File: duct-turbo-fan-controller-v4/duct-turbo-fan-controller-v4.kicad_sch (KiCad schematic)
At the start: 45 parts, among them J1 Screw_Terminal_01x04, J2 Conn_01x04, J3 USB_OTG, J4 AudioJack4, J7 Conn_01x04, Q1 MMBT3904, Q2 BSS84, SW1 SW_Push, SW2 SW_Push, U1 SCD41-D-R2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

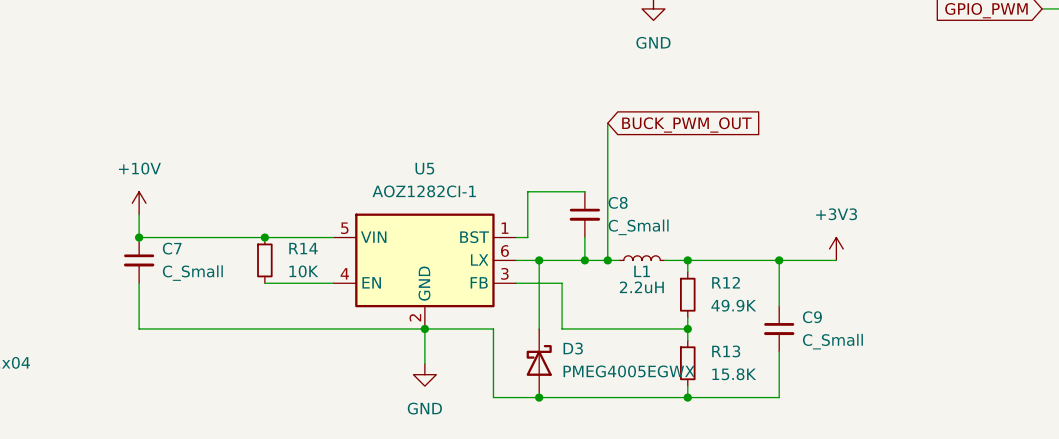
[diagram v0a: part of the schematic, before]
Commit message: Fix footprint for buck diode in schematic.
Add values for buck capacitors in schematic.
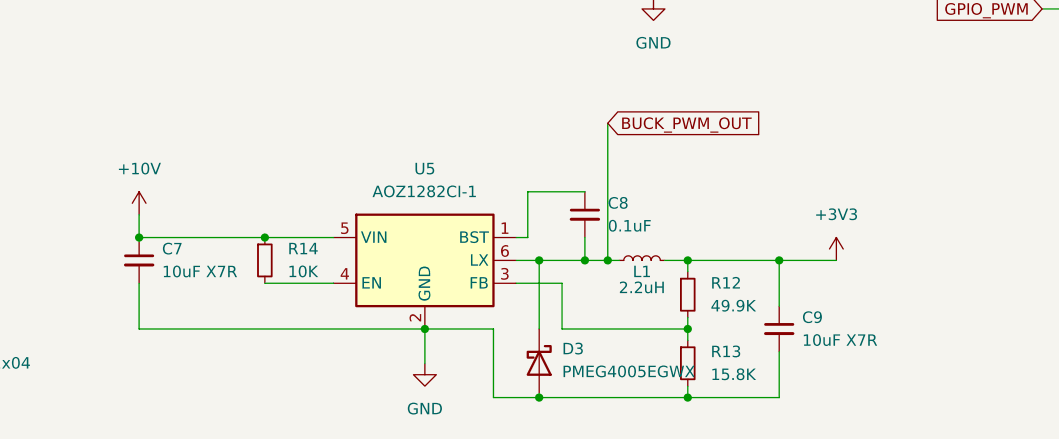
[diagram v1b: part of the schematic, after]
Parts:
- C7, C9: value C_Small -> 10uF X7R
- C8: value C_Small -> 0.1uF
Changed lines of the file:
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@@
 			)
 		)
-		(property "Value" "C_Small"
+		(property "Value" "10uF X7R"
 			(at 158.75 182.8862 0)
 			(effects
@@
 			)
 		)
-		(property "Value" "C_Small"
+		(property "Value" "0.1uF"
 			(at 137.16 170.1862 0)
 			(effects
@@
 			)
 		)
-		(property "Value" "C_Small"
+		(property "Value" "10uF X7R"
 			(at 87.63 175.2662 0)
 			(effects

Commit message: Fix buck diode footprint in pcb
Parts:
- D3: footprint Diode_SMD:D_SOD-323_HandSoldering -> Diode_SMD:D_SOD-123
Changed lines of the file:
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@@
 			)
 		)
-		(property "Footprint" "Diode_SMD:D_SOD-323_HandSoldering"
+		(property "Footprint" "Diode_SMD:D_SOD-123"
 			(at 129.54 185.42 0)
 			(effects

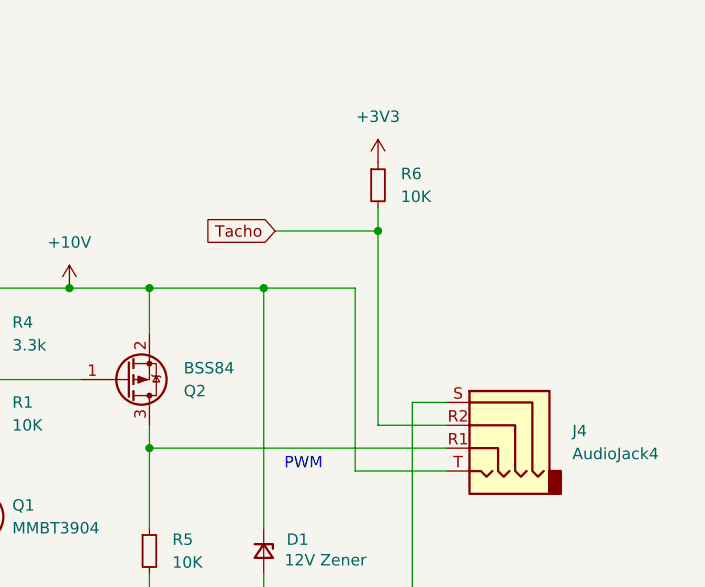
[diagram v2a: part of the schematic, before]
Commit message: Add input resistor from Tacho pin
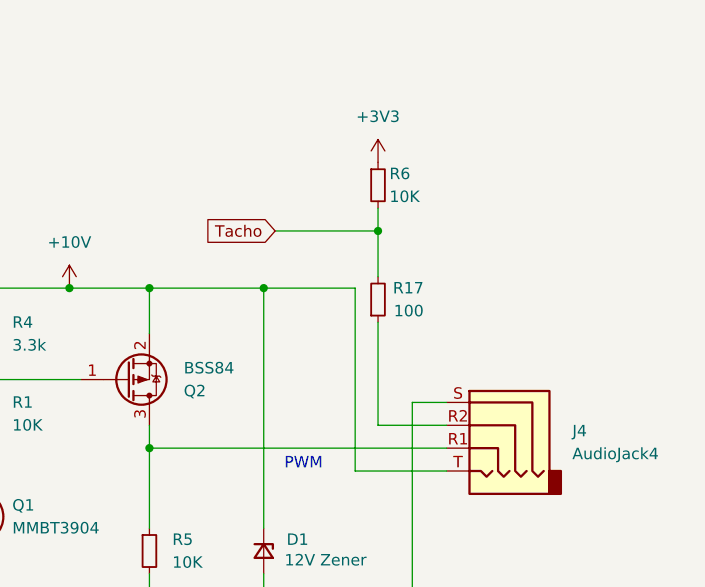
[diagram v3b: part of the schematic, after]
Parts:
- added R17: 100, Resistor_SMD:R_0603_1608Metric_Pad0.98x0.95mm_HandSolder, symbol Device:R_Small
- R6: footprint Resistor_SMD:R_0805_2012Metric_Pad1.20x1.40mm_HandSolder -> Resistor_SMD:R_0603_1608Metric_Pad0.98x0.95mm_HandSolder
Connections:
- net Tacho: now also R17.2; no longer J4.R2
- new net: J4.R2, R17.1
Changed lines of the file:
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@@
 	)
 	(junction
-		(at 142.24 125.73)
+		(at 250.19 114.3)
 		(diameter 0)
 		(color 0 0 0 0)
 	)
 	(junction
-		(at 64.77 26.67)
+		(at 142.24 125.73)
 		(diameter 0)
 		(color 0 0 0 0)
 	)
 	(junction
-		(at 204.47 44.45)
+		(at 64.77 26.67)
 		(diameter 0)
 		(color 0 0 0 0)
 	)
 	(junction
-		(at 171.45 64.77)
+		(at 204.47 44.45)
 		(diameter 0)
 		(color 0 0 0 0)
 	)
 	(junction
-		(at 250.19 114.3)
+		(at 171.45 64.77)
 		(diameter 0)
 		(color 0 0 0 0)
@@
 	(wire
 		(pts
-			(xy 238.76 114.3) (xy 250.19 114.3)
-		)
-		(stroke
-			(width 0)
-			(type default)
-		)
-	)
-	(wire
-		(pts
 			(xy 254 161.29) (xy 237.49 161.29)
 		)
@@
 	(wire
 		(pts
+			(xy 250.19 124.46) (xy 250.19 135.89)
+		)
+		(stroke
+			(width 0)
+			(type default)
+		)
+	)
+	(wire
+		(pts
 			(xy 49.53 26.67) (xy 53.34 26.67)
 		)
@@
 	(wire
 		(pts
+			(xy 250.19 114.3) (xy 250.19 119.38)
+		)
+		(stroke
+			(width 0)
+			(type default)
+		)
+	)
+	(wire
+		(pts
 			(xy 128.27 171.45) (xy 128.27 166.37)
 		)
@@
 	(wire
 		(pts
+			(xy 238.76 114.3) (xy 250.19 114.3)
+		)
+		(stroke
+			(width 0)
+			(type default)
+		)
+	)
+	(wire
+		(pts
 			(xy 196.85 154.94) (xy 196.85 161.29)
 		)
@@
 	(wire
 		(pts
-			(xy 250.19 135.89) (xy 250.19 114.3)
-		)
-		(stroke
-			(width 0)
-			(type default)
-		)
-	)
-	(wire
-		(pts
 			(xy 137.16 173.99) (xy 138.43 173.99)
 		)
@@
 		(on_board yes)
 		(dnp no)
-		(fields_autoplaced yes)
 		(property "Reference" "R6"
-			(at 252.73 107.95 0)
+			(at 251.46 107.95 0)
 			(effects
 				(font
@@
 		)
 		(property "Value" "10K"
-			(at 252.73 110.49 0)
+			(at 251.46 110.49 0)
 			(effects
 				(font
@@
 			)
 		)
-		(property "Footprint" "Resistor_SMD:R_0805_2012Metric_Pad1.20x1.40mm_HandSolder"
+		(property "Footprint" "Resistor_SMD:R_0603_1608Metric_Pad0.98x0.95mm_HandSolder"
 			(at 250.19 109.22 0)
 			(effects
@@
 					(unit 1)
 				)
+			)
+		)
+	)
+	(symbol
+		(lib_id "Device:R_Small")
+		(at 250.19 121.92 0)
+		(mirror x)
+		(unit 1)
+		(exclude_from_sim no)
+		(in_bom yes)
+		(on_board yes)
+		(dnp no)
+		(property "Reference" "R17"
+			(at 255.27 120.65 0)
+			(effects
+				(font
+					(size 1.27 1.27)
+				)
+				(justify right)
+			)
+		)
+		(property "Value" "100"
+			(at 255.27 123.19 0)
+			(effects
+				(font
+					(size 1.27 1.27)
+				)
+				(justify right)
+			)
+		)
+		(property "Footprint" "Resistor_SMD:R_0603_1608Metric_Pad0.98x0.95mm_HandSolder"
+			(at 250.19 121.92 0)
+			(effects
+				(font
+					(size 1.27 1.27)
+				)
+				(hide yes)
+			)
+		)
+		(property "Datasheet" "~"
+			(at 250.19 121.92 0)
+			(effects
+				(font
+					(size 1.27 1.27)
+				)
+				(hide yes)
+			)
+		)
+		(property "Description" ""
+			(at 250.19 121.92 0)
+			(effects
+				(font
+					(size 1.27 1.27)
+				)
+				(hide yes)
+			)
+		)
+		(pin "2"
+		)
+		(pin "1"
+		)
+		(instances
+			(project "duct-turbo-fan-controller-v4"
+				(path "/f7200693-aa8c-4dc9-bbe2-9e962fa196ea"
+					(reference "R17")
+					(unit 1)
+				)

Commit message: Fix bme688 wiring by adding +3.3V to CSB pin.
Was defaulting to spi mode and taking out the whole i2c link
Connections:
- net +3V3: now also R10.2, R11.2, U2.2 (CSB)
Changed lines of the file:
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@@
 (kicad_sch
-	(version 20231120)
+	(version 20250114)
 	(generator "eeschema")
-	(generator_version "8.0")
+	(generator_version "9.0")
 	(paper "A4")
+	(text "PWM"
+		(exclude_from_sim no)
+		(at 239.776 140.97 0)
+		(effects
+			(font
+				(size 1.27 1.27)
+			)
+			(justify left bottom)
+		)
+	)
 	(junction
 		(at 134.62 173.99)
@@
 	)
 	(junction
+		(at 181.61 69.85)
+		(diameter 0)
+		(color 0 0 0 0)
+	)
+	(junction
 		(at 64.77 36.83)
 		(diameter 0)
@@
 	(wire
 		(pts
+			(xy 210.82 69.85) (xy 210.82 66.04)
+		)
+		(stroke
+			(width 0)
+			(type default)
+		)
+	)
+	(wire
+		(pts
 			(xy 146.05 173.99) (xy 156.21 173.99)
 		)
@@
 	(wire
 		(pts
+			(xy 181.61 69.85) (xy 210.82 69.85)
+		)
+		(stroke
+			(width 0)
+			(type default)
+		)
+	)
+	(wire
+		(pts
 			(xy 254 161.29) (xy 237.49 161.29)
 		)
@@
 	(wire
 		(pts
-			(xy 152.4 46.99) (xy 152.4 40.64)
+			(xy 152.4 40.64) (xy 152.4 46.99)
 		)
 		(stroke
@@
 		)
 	)
-	(text "PWM"
-		(exclude_from_sim no)
-		(at 239.776 140.97 0)
-		(effects
-			(font
-				(size 1.27 1.27)
-			)
-			(justify left bottom)
-		)
-	)
 	(global_label "GPIO_PWM"
 		(shape input)
@@
 	(global_label "SCD41_SCA"
 		(shape input)
-		(at 69.85 87.63 0)
+		(at 69.85 87.63 180)
 		(fields_autoplaced yes)
 		(effects
@@
 				(size 1.27 1.27)
 			)
-			(justify left)
+			(justify right)
 		)
 		(property "Intersheetrefs" "${INTERSHEET_REFS}"
-			(at 83.5394 87.63 0)
+			(at 56.1606 87.63 0)
 			(effects
 				(font
 					(size 1.27 1.27)
 				)
-				(justify left)
+				(justify right)
 				(hide yes)
 			)
@@
 	)
 	(symbol
+		(lib_id "power:+3.3V")
+		(at 210.82 66.04 0)
+		(unit 1)
+		(exclude_from_sim no)
+		(in_bom yes)
+		(on_board yes)
+		(dnp no)
+		(fields_autoplaced yes)
+		(property "Reference" "#PWR028"
+			(at 210.82 69.85 0)
+			(effects
+				(font
+					(size 1.27 1.27)
+				)
+				(hide yes)
+			)
+		)
+		(property "Value" "+3V3"
+			(at 210.82 60.96 0)
+			(effects
+				(font
+					(size 1.27 1.27)
+				)
+			)
+		)
+		(property "Footprint" ""
+			(at 210.82 66.04 0)
+			(effects
+				(font
+					(size 1.27 1.27)
+				)
+				(hide yes)
+			)
+		)
+		(property "Datasheet" ""
+			(at 210.82 66.04 0)
+			(effects
+				(font
+					(size 1.27 1.27)
+				)
+				(hide yes)
+			)
+		)
+		(property "Description" ""
+			(at 210.82 66.04 0)
+			(effects
+				(font
+					(size 1.27 1.27)
+				)
+				(hide yes)
+			)
+		)
+		(pin "1"
+		)
+		(instances
+			(project "duct-turbo-fan-controller-v4"
+				(path "/f7200693-aa8c-4dc9-bbe2-9e962fa196ea"
+					(reference "#PWR028")
+					(unit 1)
+				)
+			)
+		)
+	)
+	(symbol
 		(lib_id "Device:R_Small")
 		(at 196.85 152.4 0)
@@
 		)
 	)
+	(embedded_fonts no)
 )

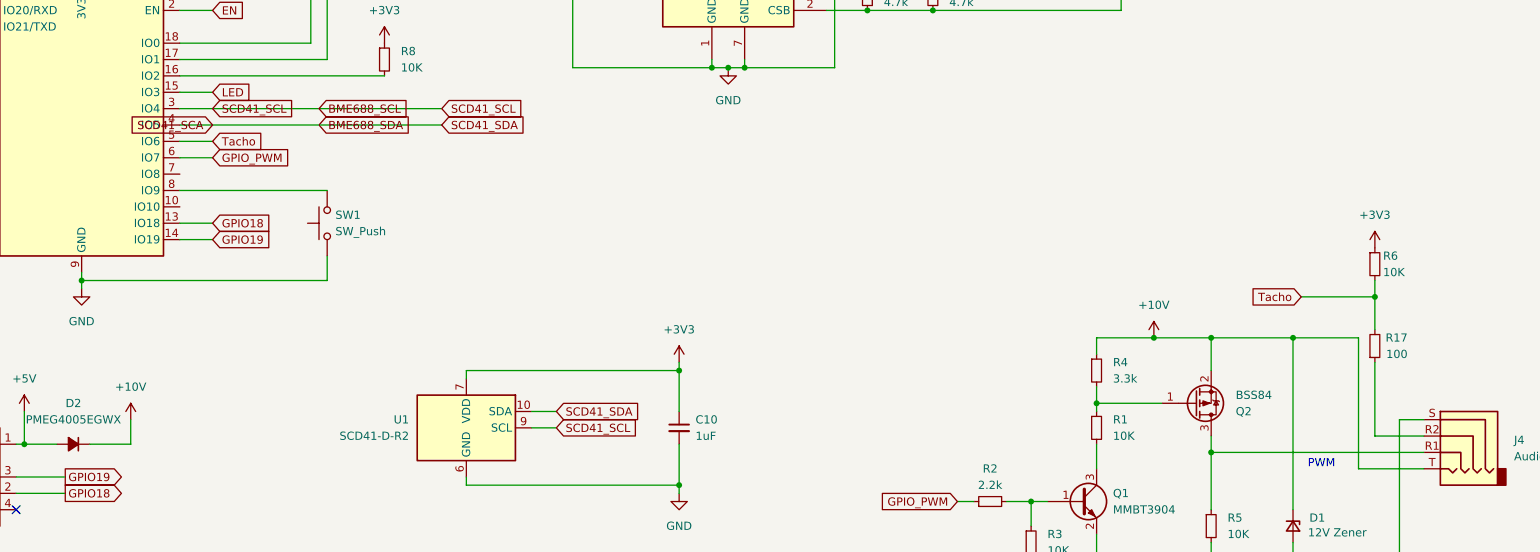
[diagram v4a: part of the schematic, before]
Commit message: Add filter capacitor to input tacho pin.
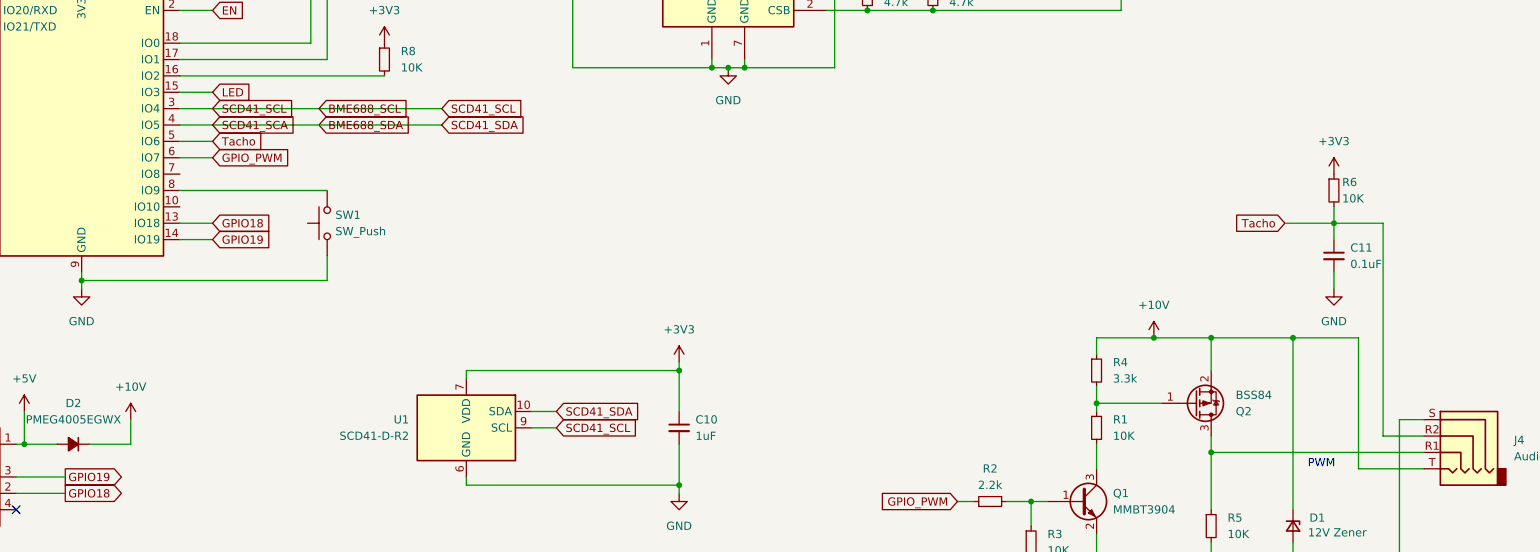
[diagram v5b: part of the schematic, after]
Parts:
- removed R17: 100, Resistor_SMD:R_0603_1608Metric_Pad0.98x0.95mm_HandSolder, symbol Device:R_Small
- added C11: 0.1uF, Capacitor_SMD:C_0603_1608Metric_Pad1.08x0.95mm_HandSolder, symbol Device:C_Small
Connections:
- net GND: now also C11.2
- net Tacho: now also J4.R2, C11.1
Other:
- moved on the sheet: R6
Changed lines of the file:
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@@
 	)
 	(junction
-		(at 250.19 114.3)
+		(at 142.24 125.73)
 		(diameter 0)
 		(color 0 0 0 0)
 	)
 	(junction
-		(at 142.24 125.73)
+		(at 64.77 26.67)
 		(diameter 0)
 		(color 0 0 0 0)
 	)
 	(junction
-		(at 64.77 26.67)
+		(at 243.84 102.87)
 		(diameter 0)
 		(color 0 0 0 0)
@@
 	(wire
 		(pts
-			(xy 250.19 124.46) (xy 250.19 135.89)
+			(xy 251.46 102.87) (xy 251.46 135.89)
+		)
+		(stroke
+			(width 0)
+			(type default)
+		)
+	)
+	(wire
+		(pts
+			(xy 243.84 102.87) (xy 251.46 102.87)
 		)
 		(stroke
@@
 	(wire
 		(pts
-			(xy 237.49 161.29) (xy 224.79 161.29)
+			(xy 243.84 102.87) (xy 243.84 105.41)
 		)
 		(stroke
@@
 	(wire
 		(pts
-			(xy 156.21 184.15) (xy 156.21 189.23)
+			(xy 237.49 161.29) (xy 224.79 161.29)
 		)
 		(stroke
@@
 	(wire
 		(pts
-			(xy 125.73 78.74) (xy 147.32 78.74)
+			(xy 156.21 184.15) (xy 156.21 189.23)
 		)
 		(stroke
@@
 	(wire
 		(pts
-			(xy 165.1 69.85) (xy 171.45 69.85)
+			(xy 125.73 78.74) (xy 147.32 78.74)
 		)
 		(stroke
@@
 	(wire
 		(pts
-			(xy 185.42 146.05) (xy 187.96 146.05)
+			(xy 165.1 69.85) (xy 171.45 69.85)
 		)
 		(stroke
@@
 	(wire
 		(pts
-			(xy 257.81 135.89) (xy 250.19 135.89)
+			(xy 185.42 146.05) (xy 187.96 146.05)
 		)
 		(stroke
@@
 	(wire
 		(pts
-			(xy 191.77 34.29) (xy 204.47 34.29)
+			(xy 257.81 135.89) (xy 251.46 135.89)
 		)
 		(stroke
@@
 	(wire
 		(pts
-			(xy 204.47 21.59) (xy 204.47 26.67)
+			(xy 191.77 34.29) (xy 204.47 34.29)
 		)
 		(stroke
@@
 	(wire
 		(pts
-			(xy 250.19 114.3) (xy 250.19 119.38)
+			(xy 204.47 21.59) (xy 204.47 26.67)
 		)
 		(stroke
@@
 	(wire
 		(pts
+			(xy 243.84 110.49) (xy 243.84 113.03)
+		)
+		(stroke
+			(width 0)
+			(type default)
+		)
+	)
+	(wire
+		(pts
 			(xy 241.3 20.32) (xy 241.3 21.59)
 		)
@@
 	(wire
 		(pts
-			(xy 238.76 114.3) (xy 250.19 114.3)
+			(xy 236.22 102.87) (xy 243.84 102.87)
 		)
 		(stroke
@@
 	(wire
 		(pts
-			(xy 250.19 111.76) (xy 250.19 114.3)
+			(xy 243.84 100.33) (xy 243.84 102.87)
 		)
 		(stroke
@@
 	(global_label "Tacho"
 		(shape input)
-		(at 238.76 114.3 180)
+		(at 236.22 102.87 180)
 		(fields_autoplaced yes)
 		(effects
@@
 		)
 		(property "Intersheetrefs" "${INTERSHEET_REFS}"
-			(at 230.2716 114.3 0)
+			(at 227.7316 102.87 0)
 			(effects
 				(font
@@
 	(global_label "SCD41_SCA"
 		(shape input)
-		(at 69.85 87.63 180)
+		(at 69.85 87.63 0)
 		(fields_autoplaced yes)
 		(effects
@@
 				(size 1.27 1.27)
 			)
-			(justify right)
+			(justify left)
 		)
 		(property "Intersheetrefs" "${INTERSHEET_REFS}"
-			(at 56.1606 87.63 0)
+			(at 83.5394 87.63 0)
 			(effects
 				(font
 					(size 1.27 1.27)
 				)
-				(justify right)
+				(justify left)
 				(hide yes)
 			)
@@
 	(symbol
 		(lib_id "power:+3.3V")
-		(at 250.19 106.68 0)
+		(at 243.84 95.25 0)
 		(unit 1)
 		(exclude_from_sim no)
@@
 		(fields_autoplaced yes)
 		(property "Reference" "#PWR05"
-			(at 250.19 110.49 0)
+			(at 243.84 99.06 0)
 			(effects
 				(font
@@
 		)
 		(property "Value" "+3V3"
-			(at 250.19 101.6 0)
+			(at 243.84 90.17 0)
 			(effects
 				(font
@@
 		)
 		(property "Footprint" ""
-			(at 250.19 106.68 0)
+			(at 243.84 95.25 0)
 			(effects
 				(font
@@
 		)
 		(property "Datasheet" ""
-			(at 250.19 106.68 0)
+			(at 243.84 95.25 0)
 			(effects
 				(font
@@
 		)
 		(property "Description" ""
-			(at 250.19 106.68 0)
+			(at 243.84 95.25 0)
 			(effects
 				(font
@@
 	(symbol
 		(lib_id "Device:R_Small")
-		(at 250.19 109.22 0)
+		(at 243.84 97.79 0)
 		(unit 1)
 		(exclude_from_sim no)
@@
 		(dnp no)
 		(property "Reference" "R6"
-			(at 251.46 107.95 0)
+			(at 245.11 96.52 0)
 			(effects
 				(font
@@
 		)
 		(property "Value" "10K"
-			(at 251.46 110.49 0)
+			(at 245.11 99.06 0)
 			(effects
 				(font
@@
 		)
 		(property "Footprint" "Resistor_SMD:R_0603_1608Metric_Pad0.98x0.95mm_HandSolder"
-			(at 250.19 109.22 0)
+			(at 243.84 97.79 0)
 			(effects
 				(font
@@
 		)
 		(property "Datasheet" "~"
-			(at 250.19 109.22 0)
+			(at 243.84 97.79 0)
 			(effects
 				(font
@@
 		)
 		(property "Description" ""
-			(at 250.19 109.22 0)
+			(at 243.84 97.79 0)
 			(effects
 				(font
@@
 	)
 	(symbol
+		(lib_id "Device:C_Small")
+		(at 243.84 107.95 0)
+		(unit 1)
+		(exclude_from_sim no)
+		(in_bom yes)
+		(on_board yes)
+		(dnp no)
+		(fields_autoplaced yes)
+		(property "Reference" "C11"
+			(at 246.38 106.6862 0)
+			(effects
+				(font
+					(size 1.27 1.27)
+				)
+				(justify left)
+			)
+		)
+		(property "Value" "0.1uF"
+			(at 246.38 109.2262 0)
+			(effects
+				(font
+					(size 1.27 1.27)
+				)
+				(justify left)
+			)
+		)
+		(property "Footprint" "Capacitor_SMD:C_0603_1608Metric_Pad1.08x0.95mm_HandSolder"
+			(at 243.84 107.95 0)
+			(effects
+				(font
+					(size 1.27 1.27)
+				)
+				(hide yes)
+			)
+		)
+		(property "Datasheet" "~"
+			(at 243.84 107.95 0)
+			(effects
+				(font
+					(size 1.27 1.27)
+				)
+				(hide yes)
+			)
+		)
+		(property "Description" "Unpolarized capacitor, small symbol"
+			(at 243.84 107.95 0)
+			(effects
+				(font
+					(size 1.27 1.27)
+				)
+				(hide yes)
+			)
+		)
+		(pin "1"
+		)
+		(pin "2"
+		)
+		(instances
+			(project "duct-turbo-fan-controller-v4"
+				(path "/f7200693-aa8c-4dc9-bbe2-9e962fa196ea"
+					(reference "C11")
+					(unit 1)
+				)
+			)
+		)
+	)
+	(symbol
 		(lib_id "power:+3.3V")
 		(at 162.56 173.99 0)
@@
 	)
 	(symbol
+		(lib_id "power:GND")
+		(at 243.84 113.03 0)
+		(unit 1)
+		(exclude_from_sim no)
+		(in_bom yes)
+		(on_board yes)
+		(dnp no)
+		(fields_autoplaced yes)
+		(property "Reference" "#PWR030"
+			(at 243.84 119.38 0)
+			(effects
+				(font
+					(size 1.27 1.27)
+				)
+				(hide yes)
+			)
+		)
+		(property "Value" "GND"
+			(at 243.84 118.11 0)
+			(effects
+				(font
+					(size 1.27 1.27)
+				)
+			)
+		)
+		(property "Footprint" ""
+			(at 243.84 113.03 0)
+			(effects
+				(font
+					(size 1.27 1.27)
+				)
+				(hide yes)
+			)
+		)
+		(property "Datasheet" ""
+			(at 243.84 113.03 0)
+			(effects
+				(font
+					(size 1.27 1.27)
+				)
+				(hide yes)
+			)
+		)
+		(property "Description" ""
+			(at 243.84 113.03 0)
+			(effects
+				(font
+					(size 1.27 1.27)
+				)
+				(hide yes)
+			)
+		)
+		(pin "1"
+		)
+		(instances
+			(project "duct-turbo-fan-controller-v4"
+				(path "/f7200693-aa8c-4dc9-bbe2-9e962fa196ea"
+					(reference "#PWR030")
+					(unit 1)
+				)
+			)
+		)
+	)
+	(symbol
 		(lib_id "Device:R_Small")
 		(at 181.61 67.31 0)
@@
 					(unit 1)
 				)
-			)
-		)
-	)
-	(symbol
-		(lib_id "Device:R_Small")
-		(at 250.19 121.92 0)
-		(mirror x)
-		(unit 1)
-		(exclude_from_sim no)
-		(in_bom yes)
-		(on_board yes)
-		(dnp no)
-		(property "Reference" "R17"
-			(at 255.27 120.65 0)
-			(effects
-				(font
-					(size 1.27 1.27)
-				)
-				(justify right)
-			)
-		)
-		(property "Value" "100"
-			(at 255.27 123.19 0)
-			(effects
-				(font
-					(size 1.27 1.27)
-				)
-				(justify right)
-			)
-		)
-		(property "Footprint" "Resistor_SMD:R_0603_1608Metric_Pad0.98x0.95mm_HandSolder"
-			(at 250.19 121.92 0)
-			(effects
-				(font
-					(size 1.27 1.27)
-				)
-				(hide yes)
-			)
-		)
-		(property "Datasheet" "~"
-			(at 250.19 121.92 0)
-			(effects
-				(font
-					(size 1.27 1.27)
-				)
-				(hide yes)
-			)
-		)
-		(property "Description" ""
-			(at 250.19 121.92 0)
-			(effects
-				(font
-					(size 1.27 1.27)
-				)
-				(hide yes)
-			)
-		)
-		(pin "2"
-		)
-		(pin "1"
-		)
-		(instances
-			(project "duct-turbo-fan-controller-v4"
-				(path "/f7200693-aa8c-4dc9-bbe2-9e962fa196ea"
-					(reference "R17")
-					(unit 1)
-				)

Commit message: Reduce size of scd41 cap to 0805
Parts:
- C10: footprint Capacitor_SMD:C_1206_3216Metric_Pad1.33x1.80mm_HandSolder -> Capacitor_SMD:C_0805_2012Metric_Pad1.18x1.45mm_HandSolder
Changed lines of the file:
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@@
 			)
 		)
-		(property "Footprint" "Capacitor_SMD:C_1206_3216Metric_Pad1.33x1.80mm_HandSolder"
+		(property "Footprint" "Capacitor_SMD:C_0805_2012Metric_Pad1.18x1.45mm_HandSolder"
 			(at 142.24 134.62 0)
 			(effects
